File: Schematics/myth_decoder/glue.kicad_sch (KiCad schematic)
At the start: 7 parts, among them U1 74HC74, U12 74LS08, U13 74AHC04, U15 4075, U19 74HC02, U2 74LS08, U3 74LS32

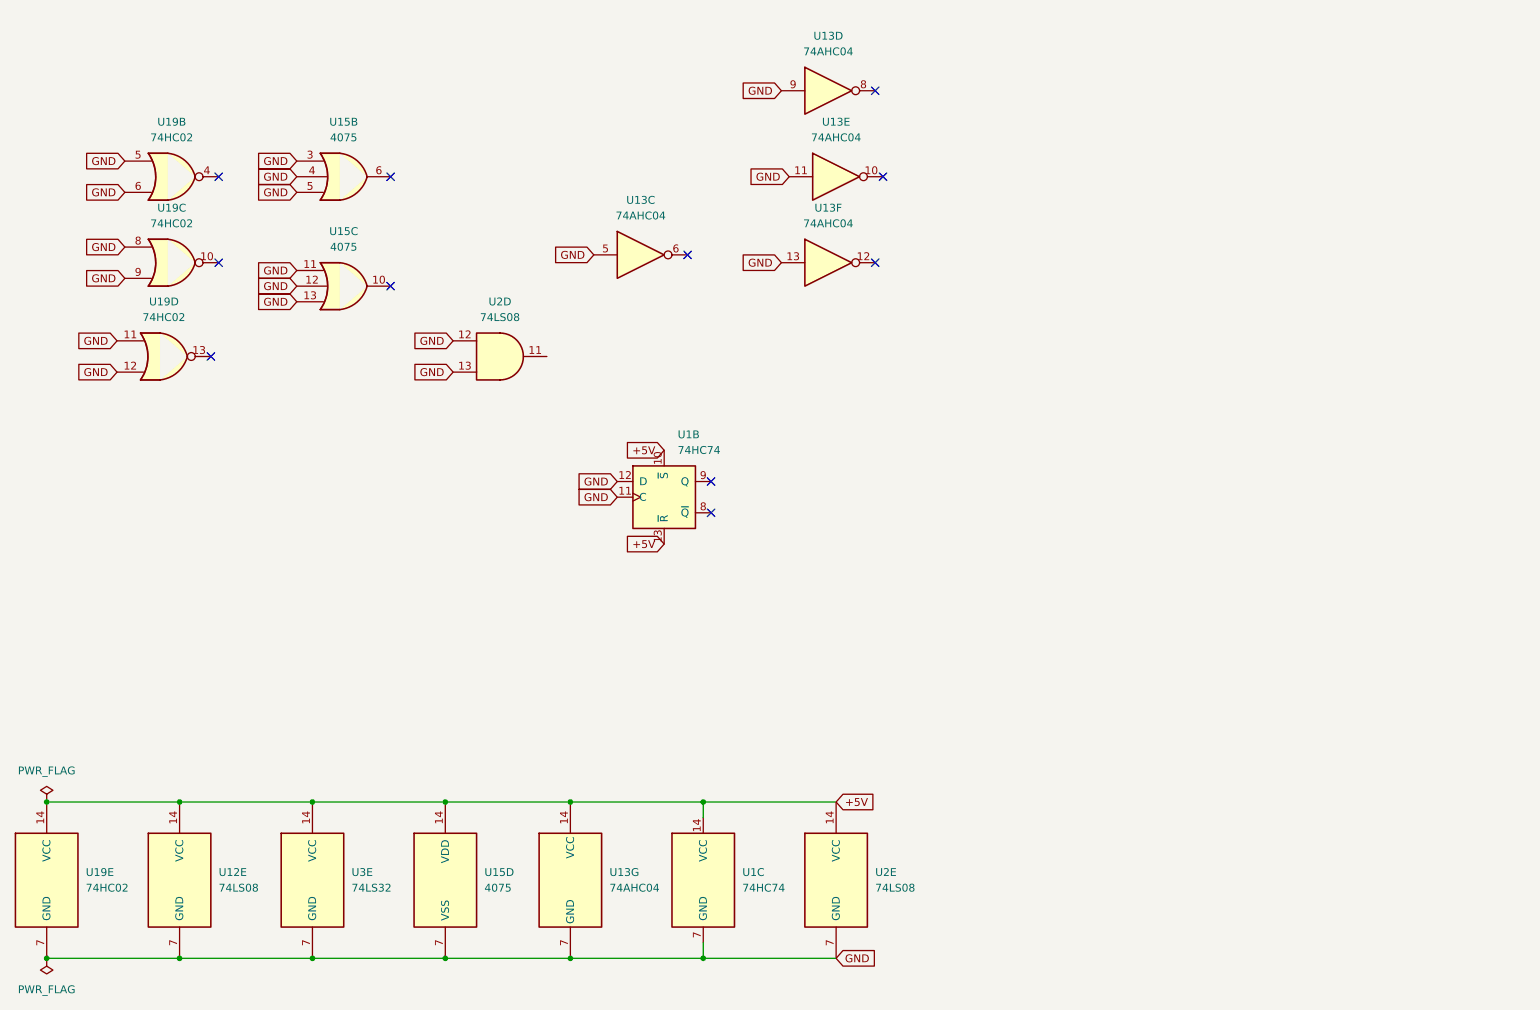
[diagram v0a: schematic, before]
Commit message: Change d to g
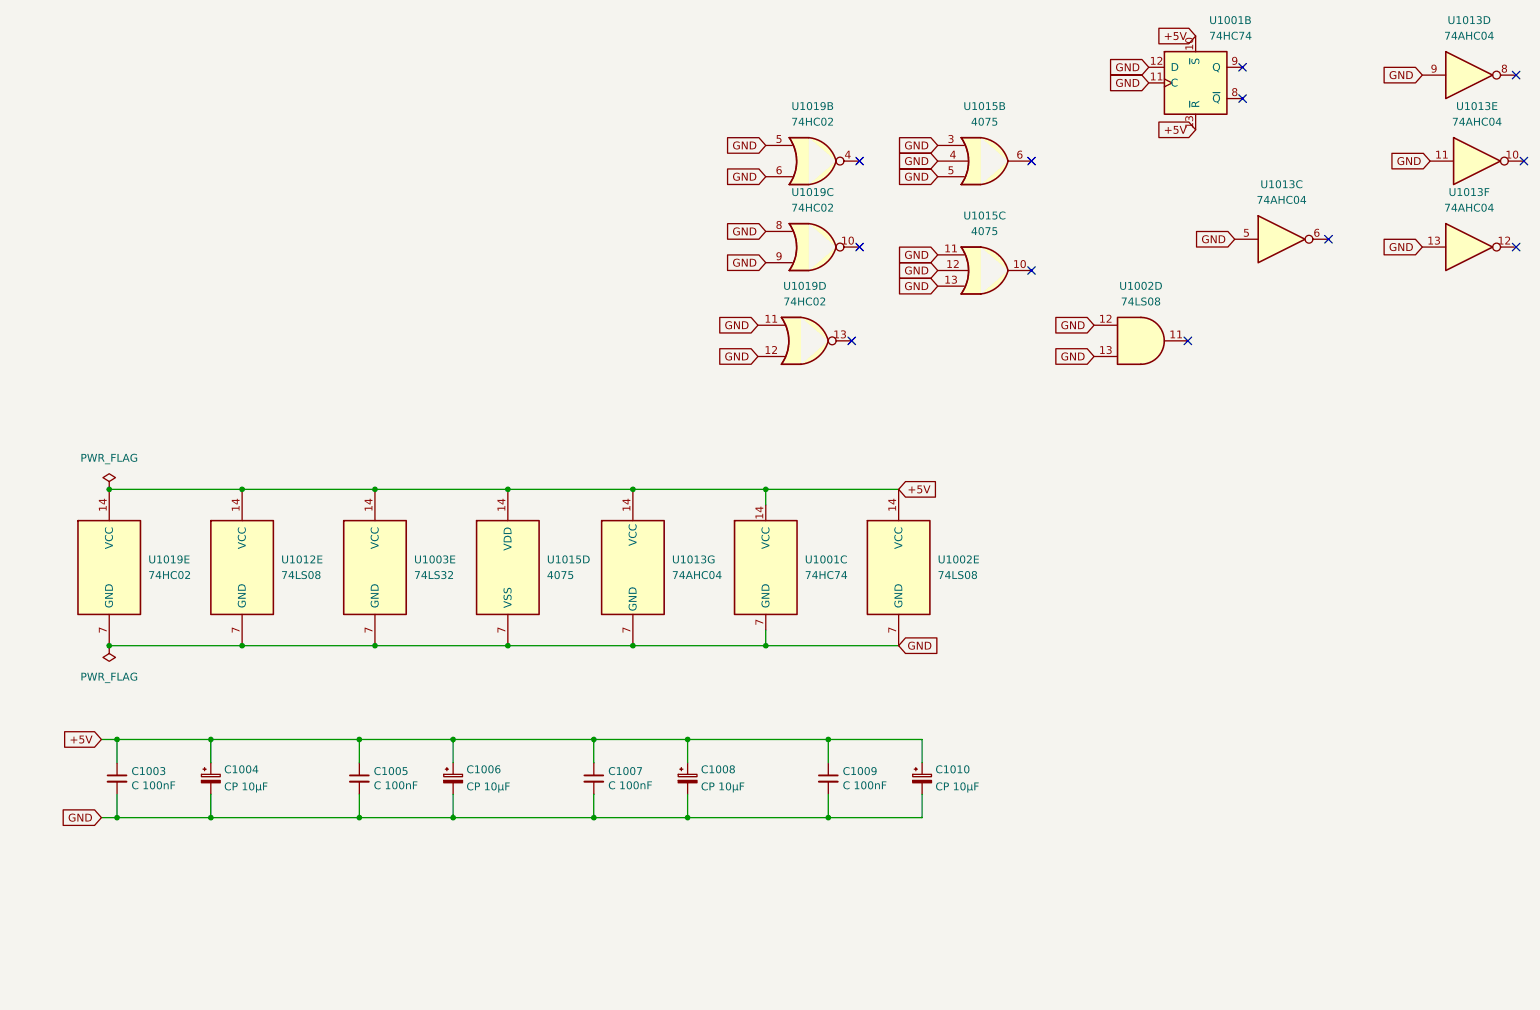
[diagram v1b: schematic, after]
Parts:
- added C1003, C1005, C1007, C1009: C 100nF, Capacitor_THT:C_Disc_D5.0mm_W2.5mm_P2.50mm, symbol Device:C_Small
- added C1004, C1006, C1008, C1010: CP 10μF, Capacitor_THT:CP_Radial_D6.3mm_P2.50mm, symbol Device:C_Polarized_Small
- renumbered U1 to U1001, U2 to U1002, U3 to U1003, U12 to U1012, U13 to U1013, U15 to U1015, U19 to U1019
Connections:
- net +5V: now also C1003.1, C1004.1, C1005.1, C1006.1, C1007.1, C1008.1, C1009.1, C1010.1
- net GND: now also C1003.2, C1004.2, C1005.2, C1006.2, C1007.2, C1008.2, C1009.2, C1010.2
- no-connect marks 11 -> 12
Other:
- moved on the sheet: U1001B, U1001C, U1002D, U1002E, U1003E, U1012E, U1013C, U1013D, U1013E, U1013F, U1013G, U1015B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

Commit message: Let defines/labels diverge from assembler mnemonics
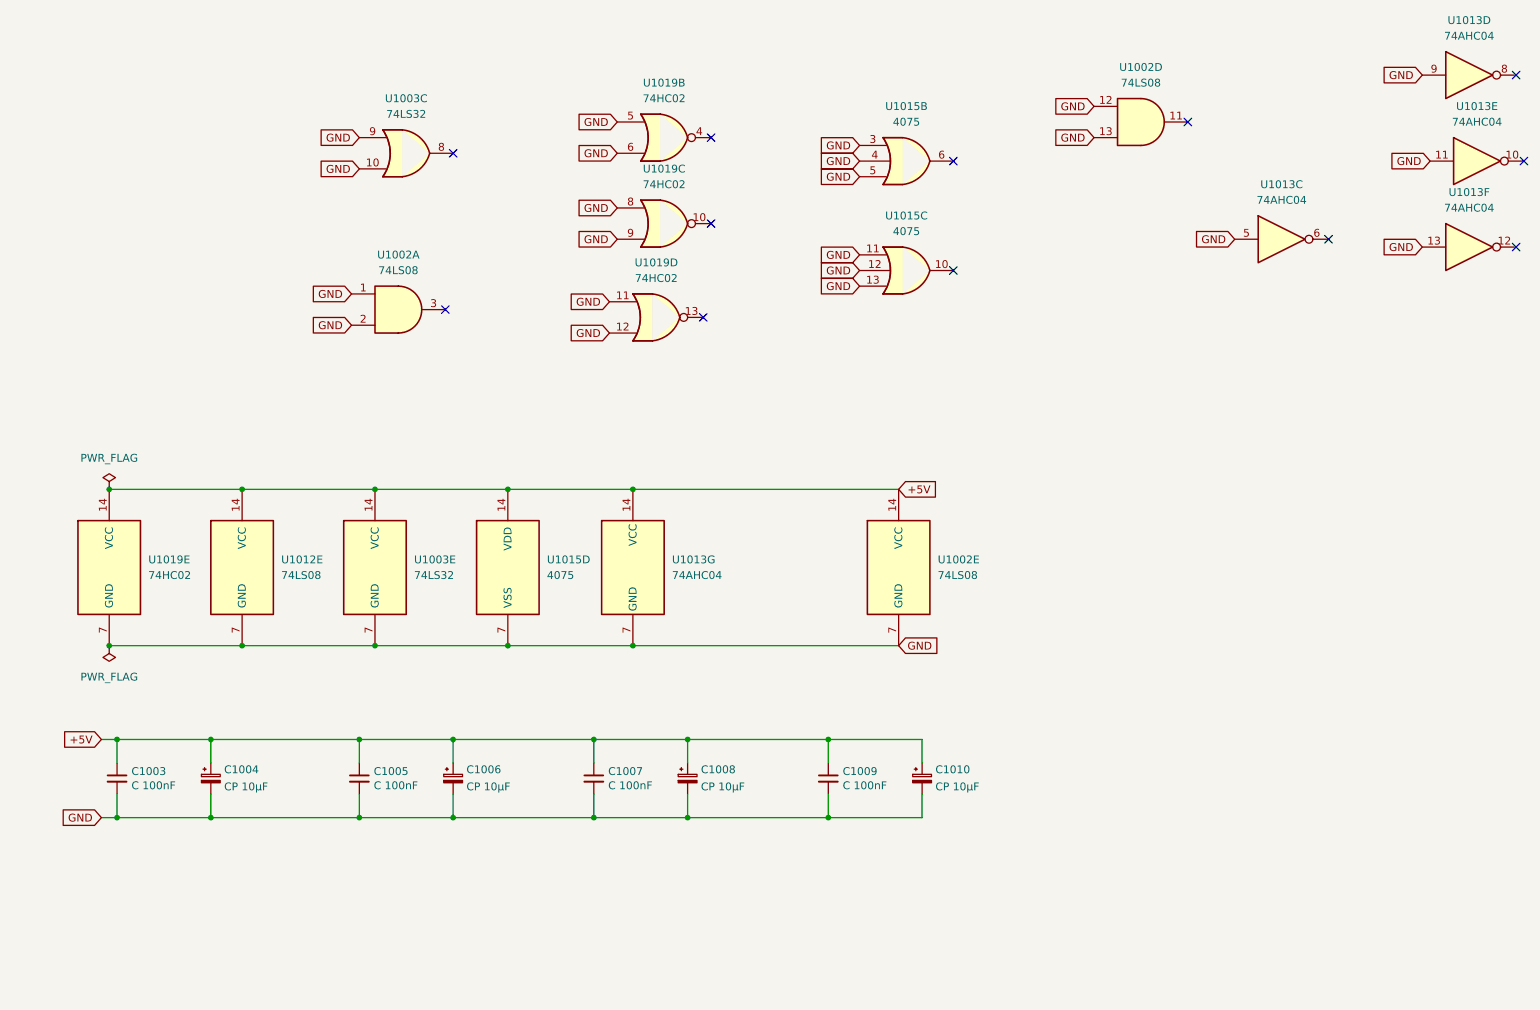
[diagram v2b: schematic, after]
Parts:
- removed U1001: 74HC74, Package_DIP:DIP-14_W7.62mm_Socket_LongPads, symbol 74xx:74HC74
- added unit 1 of U1002
- added unit 3 of U1003
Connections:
- net GND: now also U1002.1, U1002.2, U1003.10, U1003.9
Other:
- moved on the sheet: U1002D, U1015B, U1015C, U1019B, U1019C, U1019D
